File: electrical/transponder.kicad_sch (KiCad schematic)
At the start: 4 parts

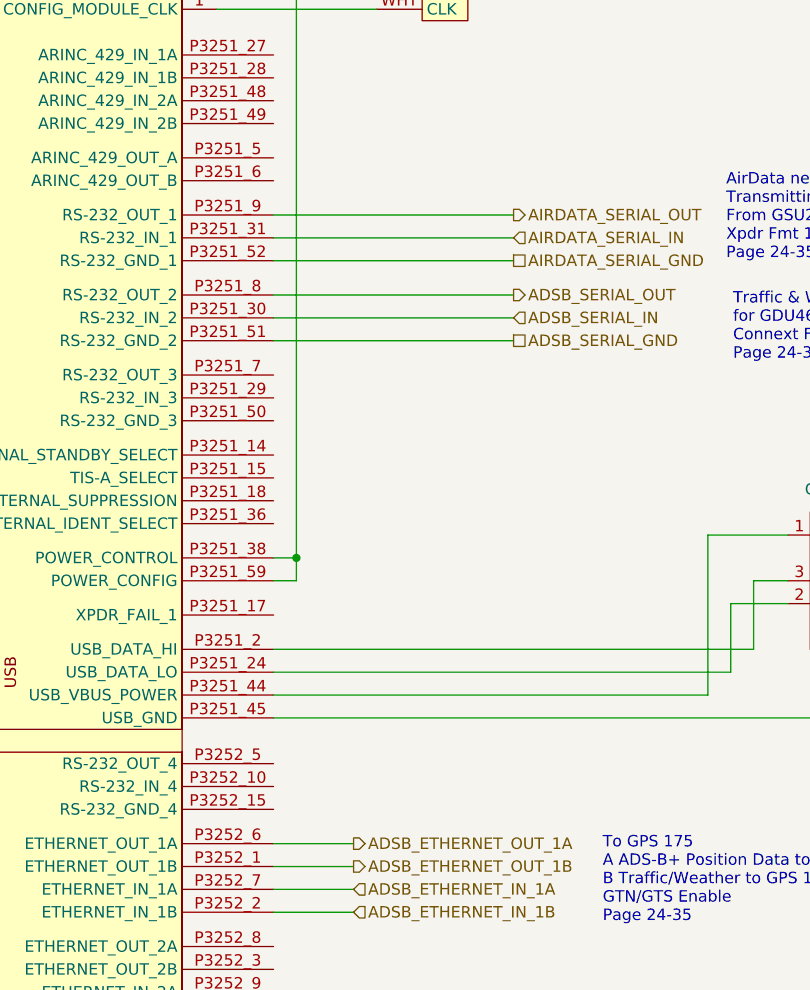
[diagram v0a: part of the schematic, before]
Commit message: Added RS232 and Canbus wiring notation
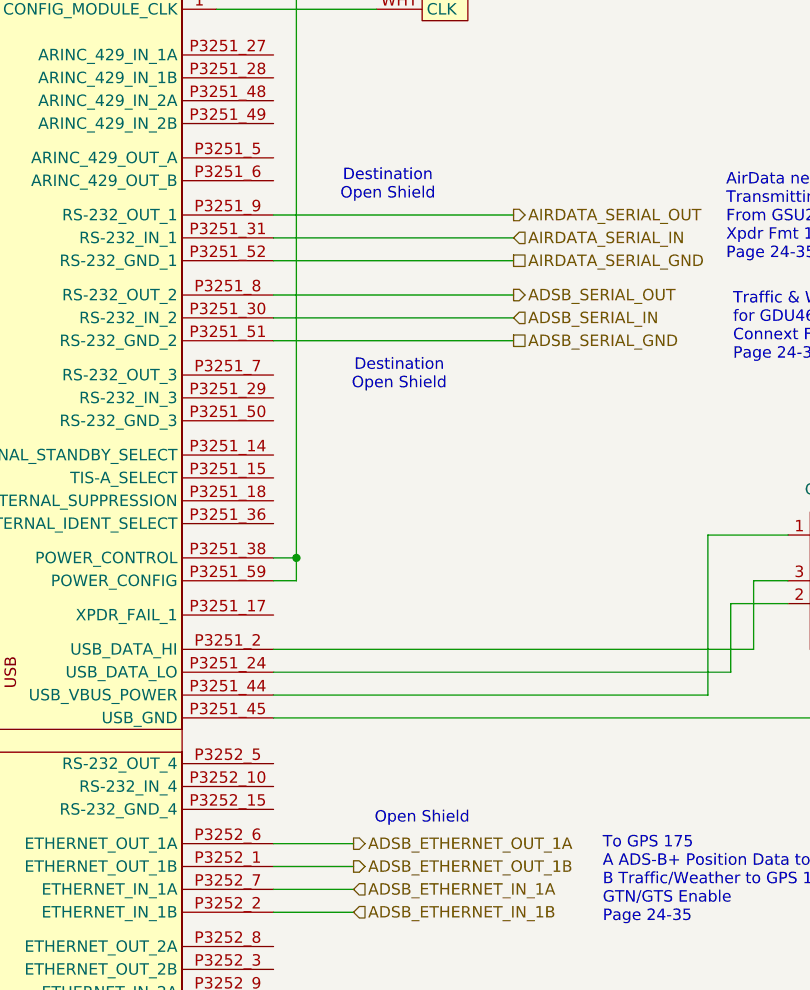
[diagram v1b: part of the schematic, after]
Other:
- note added: "Destination Open Shield"
- note added: "Open Shield"
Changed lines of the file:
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@@
 	(title_block
 		(title "Transponder")
-		(date "2025-09-08")
-		(rev "1.0")
+		(date "2025-10-02")
+		(rev "1.1.4")
 		(company "N78HR")
 	)
+	(text "Open Shield"
+		(exclude_from_sim no)
+		(at 93.98 150.876 0)
+		(effects
+			(font
+				(size 1.27 1.27)
+			)
+		)
+	)
+	(text "Destination\nOpen Shield"
+		(exclude_from_sim no)
+		(at 91.44 101.6 0)
+		(effects
+			(font
+				(size 1.27 1.27)
+			)
+		)
+	)
+	(text "Destination\nOpen Shield"
+		(exclude_from_sim no)
+		(at 90.17 80.518 0)
+		(effects
+			(font
+				(size 1.27 1.27)
+			)
+		)
+	)
 	(text "Traffic & Weather Out\nfor GDU460\nConnext Fmt 4\nPage 24-35"

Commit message: Added lighting bus
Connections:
- new net LIGHTS_HI: GTX345.P3251_19 (LIGHTING_BUS_HI)
- no-connect marks 0 -> 1
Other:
- moved on the sheet: GTX45R_CONFIG, GTX45R_USB, XPDR_ANT

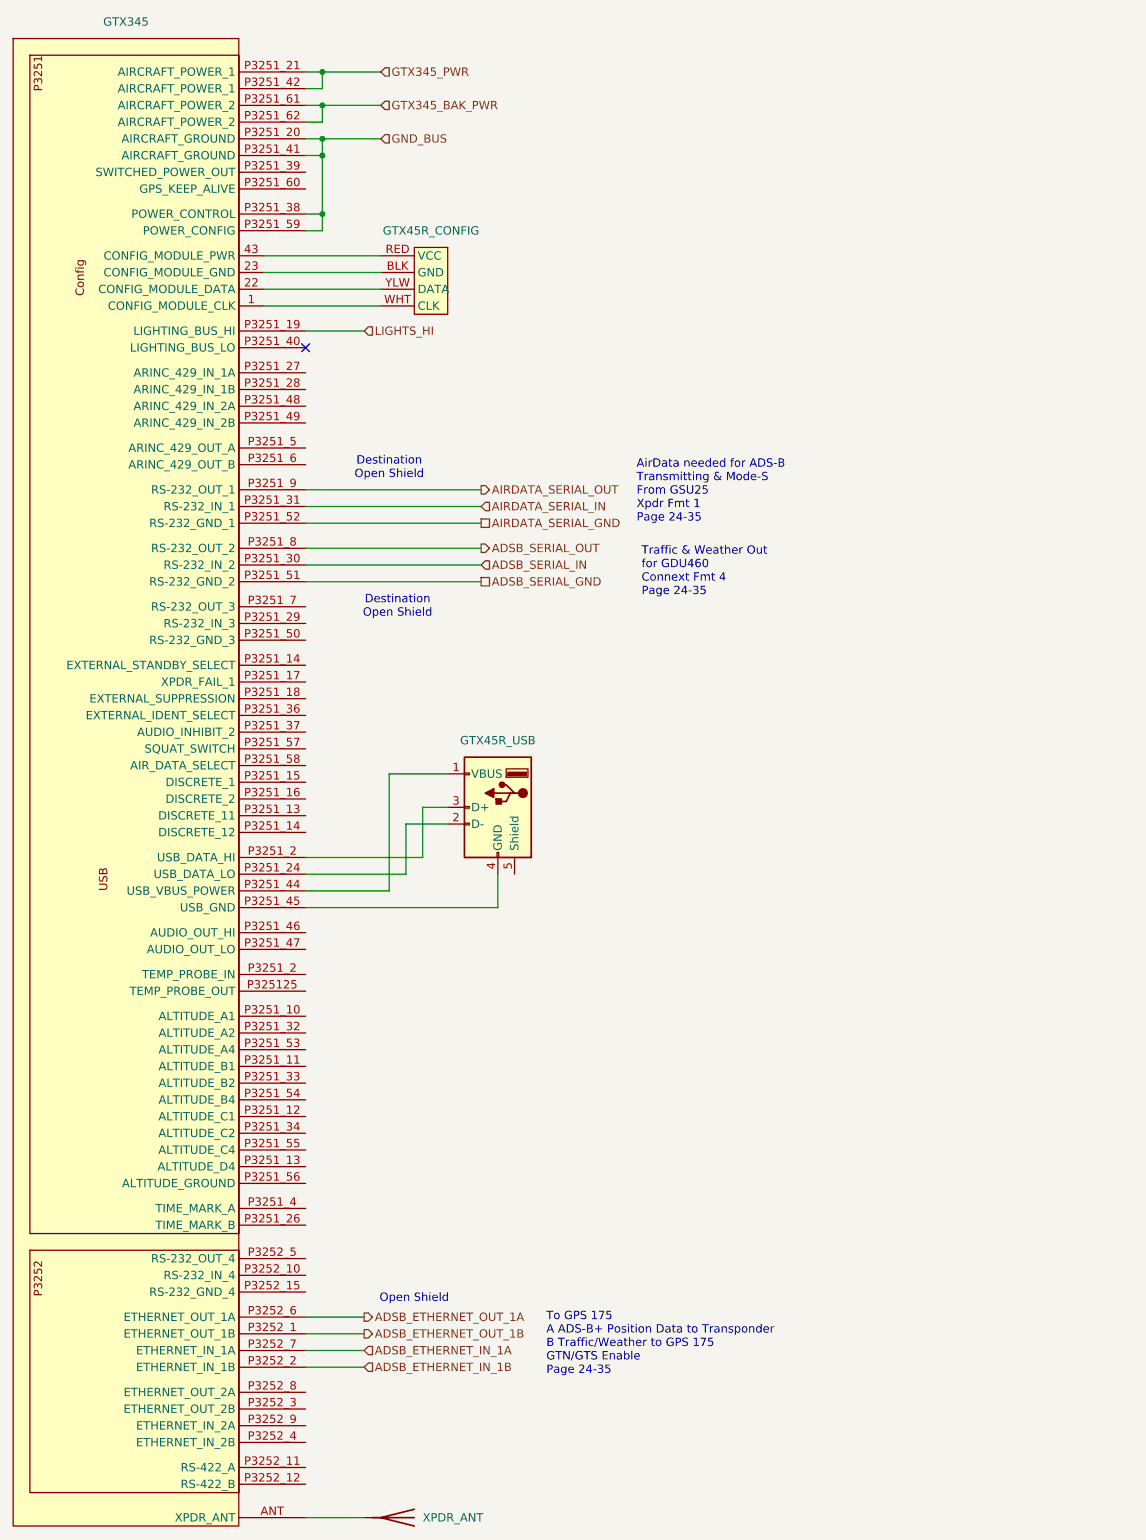
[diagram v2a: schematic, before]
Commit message: Removed power config. Added USB-B plug for GTX 345 to GSB 15.
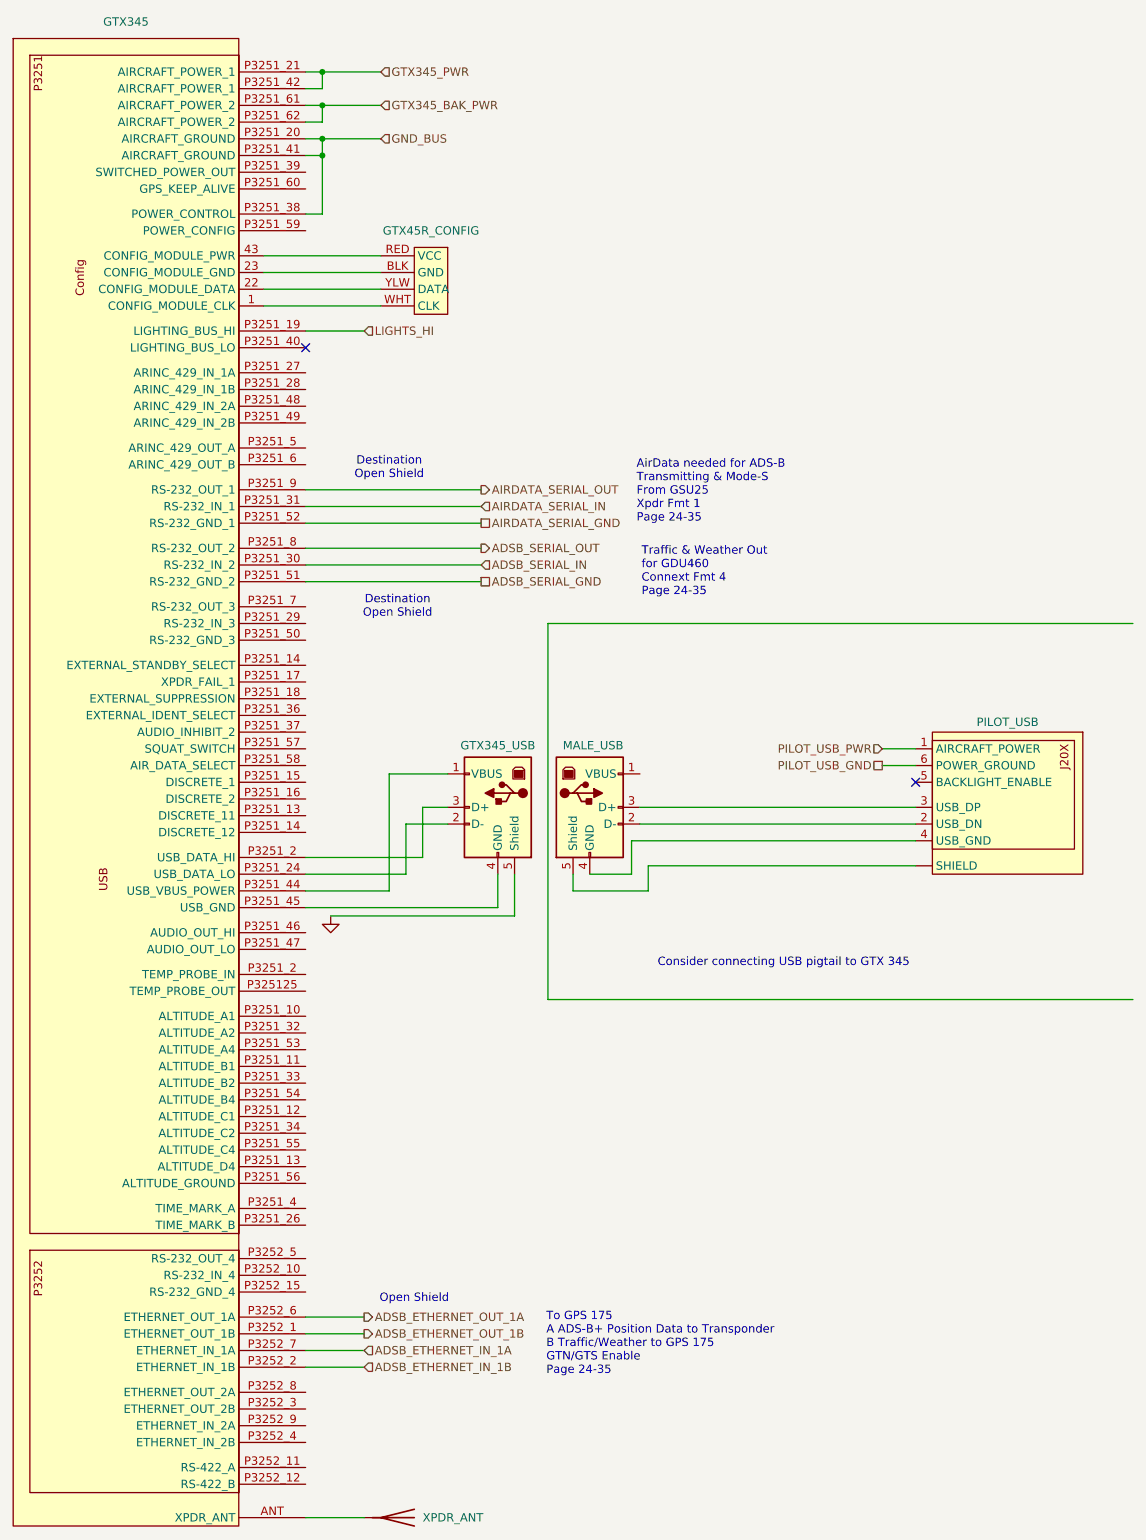
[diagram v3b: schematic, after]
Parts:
- removed GTX45R_USB: USB_A, symbol Connector:USB_A
- added GTX345_USB, MALE_USB: USB_B, symbol Connector:USB_B
- added PILOT_USB: ~, symbol flyerx:Garmin_GSB15
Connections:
- net GND_BUS: no longer GTX345.P3251_59 (POWER_CONFIG)
- net at GTX345.P3251_44 (USB_VBUS_POWER): now also GTX345_USB.1 (VBUS)
- net at GTX345.P3251_24 (USB_DATA_LO): now also GTX345_USB.2 (D-)
- net at GTX345.P3251_45 (USB_GND): now also GTX345_USB.4 (GND)
- new net: MALE_USB.2 (D-), PILOT_USB.2 (USB_DN)
- new net: MALE_USB.3 (D+), PILOT_USB.3 (USB_DP)
- new net: MALE_USB.4 (GND), PILOT_USB.4 (USB_GND)
- new net: MALE_USB.5 (Shield), PILOT_USB. (SHIELD)
- new net: GTX345.P3251_2 (TEMP_PROBE_IN), GTX345_USB.3 (D+)
- new net GNDS: GTX345_USB.5 (Shield)
- new net PILOT_USB_GND: PILOT_USB.6 (POWER_GROUND)
- new net PILOT_USB_PWR: PILOT_USB.1 (AIRCRAFT_POWER)
- no-connect marks 1 -> 2
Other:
- note added: "Consider connecting USB pigtail to GTX 345"

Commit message: Added shielding and wire colors and corrections.
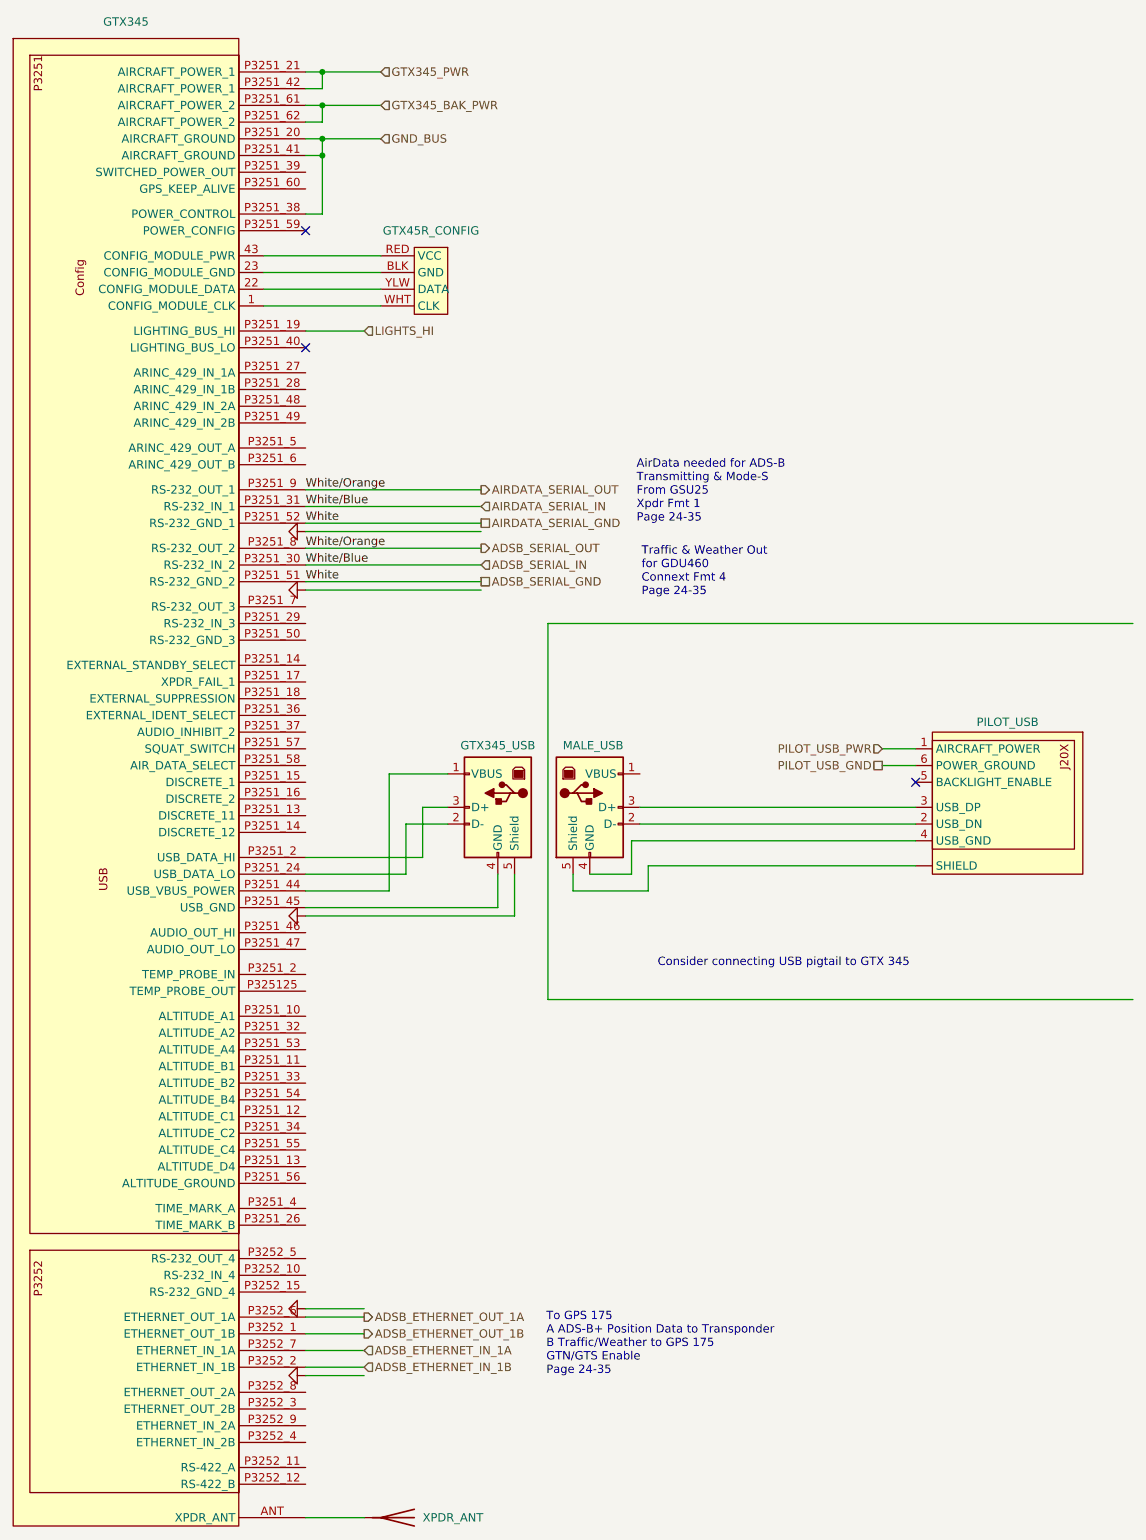
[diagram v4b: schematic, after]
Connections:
- net AIRDATA_SERIAL_GND is gone; now on net ADSB_SERIAL_GND: GTX345.P3251_52 (RS-232_GND_1)
- net AIRDATA_SERIAL_IN is gone; now on net ADSB_SERIAL_IN: GTX345.P3251_31 (RS-232_IN_1)
- net AIRDATA_SERIAL_OUT is gone; now on net ADSB_SERIAL_OUT: GTX345.P3251_9 (RS-232_OUT_1)
- no-connect marks 2 -> 3
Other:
- note removed: "Destination Open Shield"
- note removed: "Open Shield"
